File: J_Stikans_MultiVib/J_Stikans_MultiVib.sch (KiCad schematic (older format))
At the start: 11 parts

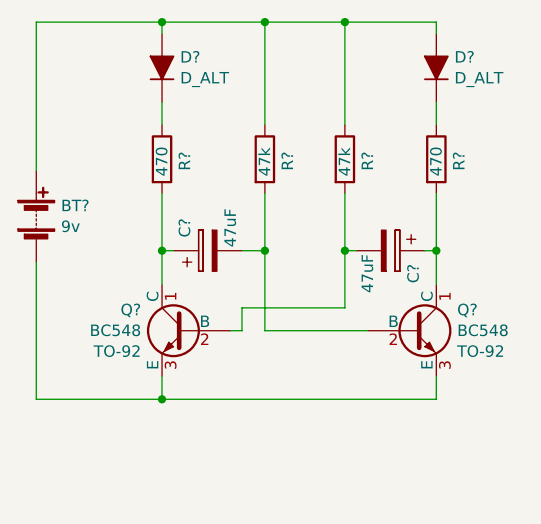
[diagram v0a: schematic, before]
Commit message: Multivibrator schematic modification with the new symbol + some corrections
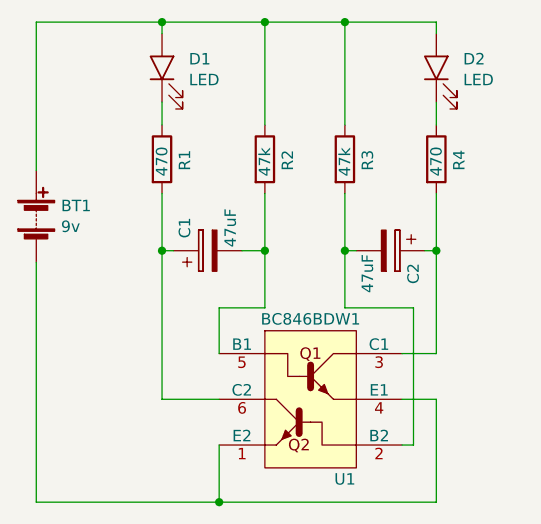
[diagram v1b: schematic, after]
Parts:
- removed D? (x2): D_ALT, symbol Device:D_ALT
- removed Q? (x2): BC548, symbol Custom_Lib_1:Q_NPN_CBE
- added D1, D2: LED, symbol Custom_Lib_1:LED
- added U1: BC846BDW1, symbol Custom_Lib_1:BC846BDW1
- gave numbers to parts that had none: 7
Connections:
- net at BT1.1 (+), R2.1, R3.1: now also D1.2 (A), D2.2 (A)
- net at BT1.2 (-): now also U1.1 (E2), U1.4 (E1)
- net at C1.2, R2.2: now also U1.5 (B1)
- net at R1.1: now also D1.1 (K)
- net at R4.1: now also D2.1 (K)
- net at C1.1, R1.2: now also U1.6 (C2)
- net at C2.2, R3.2: now also U1.2 (B2)
- net at C2.1, R4.2: now also U1.3 (C1)
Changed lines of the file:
@@
 $EndDescr
 $Comp
-L Device:Battery BT?
+L Device:Battery BT1
 U 1 1 5F7E2DEA
 P 3550 3300
-F 0 "BT?" H 3658 3346 50  0000 L CNN
+F 0 "BT1" H 3658 3346 50  0000 L CNN
 F 1 "9v" H 3658 3255 50  0000 L CNN
 F 2 "" V 3550 3360 50  0001 C CNN
@@
 $EndComp
 $Comp
-L Device:R R?
+L Device:R R2
 U 1 1 5F7E2EBE
 P 4550 3050
-F 0 "R?" V 4650 3000 50  0000 L CNN
+F 0 "R2" V 4650 3000 50  0000 L CNN
 F 1 "47k" V 4550 2975 50  0000 L CNN
 F 2 "" V 4480 3050 50  0001 C CNN
@@
 $EndComp
 $Comp
-L Device:D_ALT D?
-U 1 1 5F7E2F68
-P 4100 2650
-F 0 "D?" V 4146 2571 50  0000 R CNN
-F 1 "D_ALT" V 4055 2571 50  0000 R CNN
-F 2 "" H 4100 2650 50  0001 C CNN
-F 3 "~" H 4100 2650 50  0001 C CNN
-	1    4100 2650
-	0    -1   -1   0
-$EndComp
-$Comp
-L Device:D_ALT D?
-U 1 1 5F7E3001
-P 5300 2650
-F 0 "D?" V 5346 2571 50  0000 R CNN
-F 1 "D_ALT" V 5255 2571 50  0000 R CNN
-F 2 "" H 5300 2650 50  0001 C CNN
-F 3 "~" H 5300 2650 50  0001 C CNN
-	1    5300 2650
-	0    -1   -1   0
-$EndComp
-$Comp
-L Device:CP C?
+L Device:CP C1
 U 1 1 5F7E3078
 P 4300 3450
-F 0 "C?" H 4400 3550 50  0000 C CNN
+F 0 "C1" H 4400 3550 50  0000 C CNN
 F 1 "47uF" H 4400 3350 50  0000 C CNN
 F 2 "" H 4338 3300 50  0001 C CNN
@@
 	1    4300 3450
 	0    -1   -1   0
-$EndComp
-Wire Wire Line
-	3550 3500 3550 4100
-Wire Wire Line
-	3550 4100 4100 4100
-Wire Wire Line
-	5300 4100 5300 4000
-Wire Wire Line
-	4100 4000 4100 4100
-Connection ~ 4100 4100
-Wire Wire Line
-	4100 4100 5300 4100
-$Comp
-L Custom_Lib_1:Q_NPN_CBE Q?
-U 1 1 5F7E37AC
-P 4200 3800
-F 0 "Q?" H 4391 3891 50  0000 L CNN
-F 1 "BC548" H 4391 3800 50  0000 L CNN
-F 2 "" H 4400 3900 50  0001 C CNN
-F 3 "~" H 4200 3800 50  0001 C CNN
-F 4 "TO-92" H 4391 3709 50  0000 L CNN "Field4"
-	1    4200 3800
-	-1   0    0    -1
 $EndComp
 Wire Wire Line
@@
 Connection ~ 4100 3450
 Wire Wire Line
-	4100 3450 4100 3600
-Wire Wire Line
 	5250 3450 5300 3450
-Wire Wire Line
-	5300 3450 5300 3600
 Wire Wire Line
 	5300 3200 5300 3450
@@
 	4900 3200 4900 3450
 Wire Wire Line
-	4900 3700 4450 3700
-Wire Wire Line
 	4550 3200 4550 3450
 Wire Wire Line
-	4550 3800 5000 3800
-Wire Wire Line
-	4450 3700 4450 3800
-Wire Wire Line
-	4450 3800 4400 3800
-Wire Wire Line
 	4450 3450 4550 3450
-Connection ~ 4550 3450
-Wire Wire Line
-	4550 3450 4550 3800
 Wire Wire Line
 	4950 3450 4900 3450
-Connection ~ 4900 3450
-Wire Wire Line
-	4900 3450 4900 3700
 $Comp
-L Device:R R?
+L Device:R R1
 U 1 1 5F7E6084
 P 4100 3050
-F 0 "R?" V 4200 3000 50  0000 L CNN
+F 0 "R1" V 4200 3000 50  0000 L CNN
 F 1 "470" V 4100 2975 50  0000 L CNN
 F 2 "" V 4030 3050 50  0001 C CNN
@@
 $EndComp
 $Comp
-L Device:R R?
+L Device:R R3
 U 1 1 5F7E60B8
 P 4900 3050
-F 0 "R?" V 5000 3000 50  0000 L CNN
+F 0 "R3" V 5000 3000 50  0000 L CNN
 F 1 "47k" V 4900 2975 50  0000 L CNN
 F 2 "" V 4830 3050 50  0001 C CNN
@@
 $EndComp
 $Comp
-L Device:R R?
+L Device:R R4
 U 1 1 5F7E613C
 P 5300 3050
-F 0 "R?" V 5400 3000 50  0000 L CNN
+F 0 "R4" V 5400 3000 50  0000 L CNN
 F 1 "470" V 5300 2975 50  0000 L CNN
 F 2 "" V 5230 3050 50  0001 C CNN
@@
 $EndComp
 $Comp
-L Device:CP C?
+L Device:CP C2
 U 1 1 5F7E6441
 P 5100 3450
-F 0 "C?" H 5200 3550 50  0000 C CNN
+F 0 "C2" H 5200 3550 50  0000 C CNN
 F 1 "47uF" H 5200 3350 50  0000 C CNN
 F 2 "" H 5138 3300 50  0001 C CNN
@@
 $EndComp
 $Comp
-L Custom_Lib_1:Q_NPN_CBE Q?
-U 1 1 5F7ED690
-P 5200 3800
-F 0 "Q?" H 5391 3891 50  0000 L CNN
-F 1 "BC548" H 5391 3800 50  0000 L CNN
-F 2 "" H 5400 3900 50  0001 C CNN
-F 3 "~" H 5200 3800 50  0001 C CNN
-F 4 "TO-92" H 5391 3709 50  0000 L CNN "Field4"
-	1    5200 3800
+L Custom_Lib_1:BC846BDW1 U1
+U 1 1 5F7EEB22
+P 4800 3900
+F 0 "U1" H 4900 3350 50  0000 C CNN
+F 1 "BC846BDW1" H 4750 4050 50  0000 C CNN
+F 2 "" H 4850 3900 50  0001 C CNN
+F 3 "" H 4850 3900 50  0001 C CNN
+	1    4800 3900
 	1    0    0    -1
 $EndComp
+Wire Wire Line
+	4350 3900 4350 3700
+Wire Wire Line
+	4350 3700 4550 3700
+Wire Wire Line
+	4550 3700 4550 3450
+Connection ~ 4550 3450
+Wire Wire Line
+	4900 3450 4900 3700
+Connection ~ 4900 3450
+Wire Wire Line
+	4100 3450 4100 4100
+Wire Wire Line
+	4100 4100 4350 4100
+Wire Wire Line
+	5300 3450 5300 3900
+Wire Wire Line
+	5150 4100 5300 4100
+Wire Wire Line
+	5300 4100 5300 4550
+Wire Wire Line
+	5300 4550 4350 4550
+Wire Wire Line
+	3550 3500 3550 4550
+Wire Wire Line
+	4350 4300 4350 4550
+Connection ~ 4350 4550
+Wire Wire Line
+	4350 4550 3550 4550
+Wire Wire Line
+	5150 3900 5300 3900
+Wire Wire Line
+	5200 3700 5200 4300
+Wire Wire Line
+	5200 4300 5150 4300
+Wire Wire Line
+	4900 3700 5200 3700
+$Comp
+L Custom_Lib_1:LED D1
+U 1 1 5F8008B0
+P 4100 2650
+F 0 "D1" V 4138 2533 50  0000 R CNN
+F 1 "LED" V 4047 2533 50  0000 R CNN
+F 2 "" H 4100 2650 50  0001 C CNN
+F 3 "~" H 4100 2650 50  0001 C CNN
+	1    4100 2650
+	0    -1   -1   0
+$EndComp
+$Comp
+L Custom_Lib_1:LED D2
+U 1 1 5F800998
+P 5300 2650
+F 0 "D2" V 5338 2533 50  0000 R CNN
+F 1 "LED" V 5247 2533 50  0000 R CNN
+F 2 "" H 5300 2650 50  0001 C CNN
+F 3 "~" H 5300 2650 50  0001 C CNN
+	1    5300 2650
+	0    -1   -1   0
+$EndComp
 $EndSCHEMATC
